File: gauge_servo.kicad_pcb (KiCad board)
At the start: 4 copper layers, 82 x 70 mm, 41 parts, among them J1 Servo 1, J10 LIM1, J11 LIM2, J12 NPX1, J3 Servo 2, J4 I2C, J5 STEPPER, J6 INPUT_1, J7 NPX2, J8 INPUT_2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

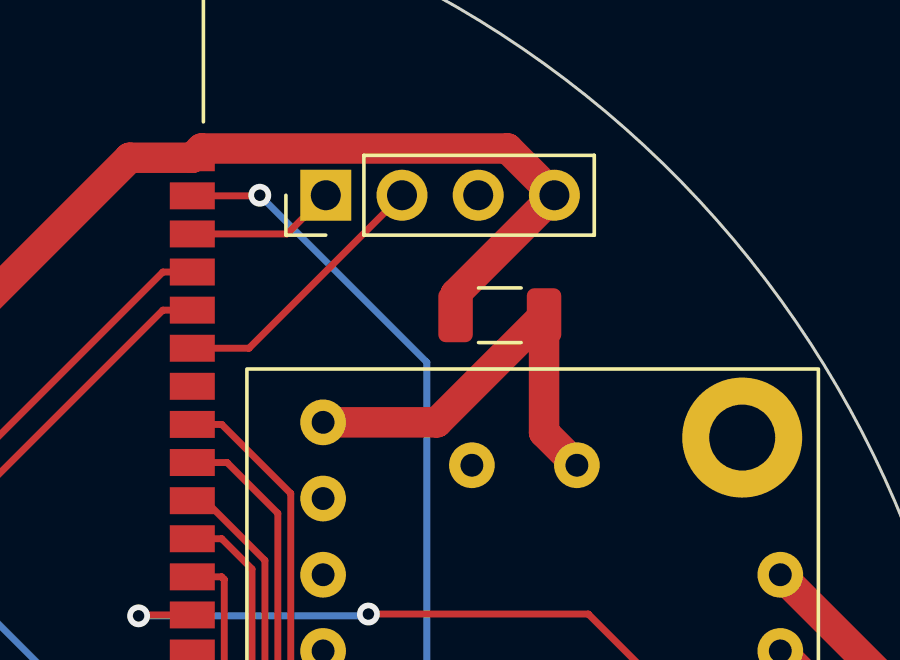
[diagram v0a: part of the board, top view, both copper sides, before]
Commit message: Fixed pinout error or Adafruit TB6612 custom component that caused short between 5V and gnd
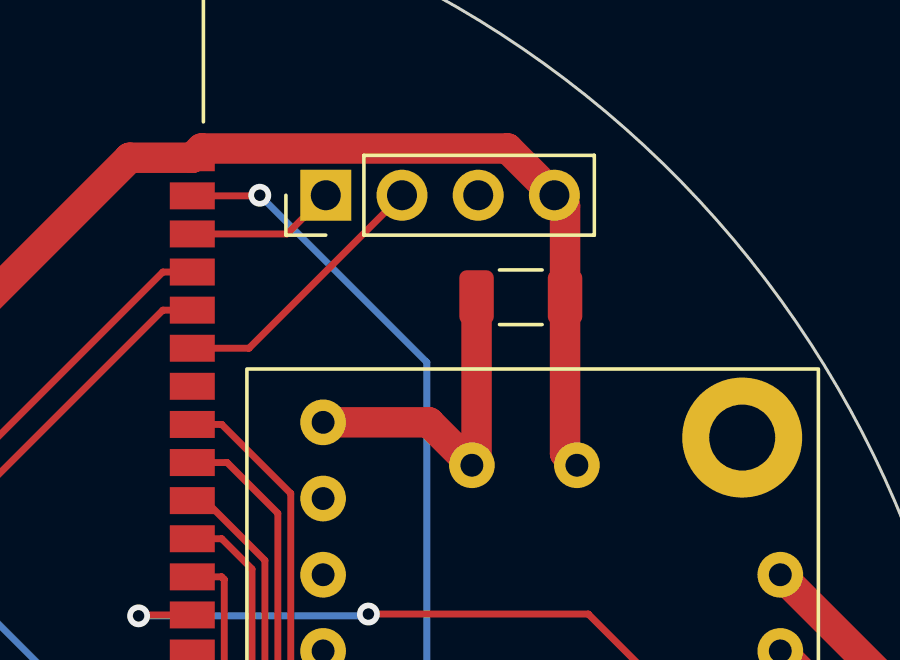
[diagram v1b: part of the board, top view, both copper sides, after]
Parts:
- moved C4 0.92 mm to (169.7, 79.4), turned to 0 degrees
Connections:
- U3 pad 17: +5V -> GND
- U3 pad 18: GND -> +5V
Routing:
- net GND: track 108.9 -> 112.9 mm
- net +5V: track 90.3 -> 87.2 mm
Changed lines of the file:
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@@
   )
   (footprint "Capacitor_SMD:C_1206_3216Metric" (layer "F.Cu")
-    (at 169 80 180)
+    (at 169.7 79.4)
     (descr "Capacitor SMD 1206 (3216 Metric), square (rectangular) end terminal, IPC_7351 nominal, (Body size source: IPC-SM-782 page 76, https://www.pcb-3d.com/wordpress/wp-content/uploads/ipc-sm-782a_amendment_1_and_2.pdf), generated with kicad-footprint-generator")
     (tags "capacitor")
@@
     (fp_line (start 1.6 -0.8) (end 1.6 0.8) (layer "F.Fab") (width 0.1))
     (fp_line (start -1.6 -0.8) (end 1.6 -0.8) (layer "F.Fab") (width 0.1))
-    (pad "1" smd roundrect (at -1.475 0 180) (size 1.15 1.8) (layers "F.Cu" "F.Paste" "F.Mask") (roundrect_rratio 0.217391)
+    (pad "1" smd roundrect (at -1.475 0) (size 1.15 1.8) (layers "F.Cu" "F.Paste" "F.Mask") (roundrect_rratio 0.217391)
       (net 3 "+5V") (pintype "passive"))
-    (pad "2" smd roundrect (at 1.475 0 180) (size 1.15 1.8) (layers "F.Cu" "F.Paste" "F.Mask") (roundrect_rratio 0.217391)
+    (pad "2" smd roundrect (at 1.475 0) (size 1.15 1.8) (layers "F.Cu" "F.Paste" "F.Mask") (roundrect_rratio 0.217391)
       (net 2 "GND") (pintype "passive"))
     (model "${KICAD6_3DMODEL_DIR}/Capacitor_SMD.3dshapes/C_1206_3216Metric.wrl"
@@
       (net 45 "Net-(J5-Pad4)") (pinfunction "MOTOR_B1") (pintype "output"))
     (pad "17" thru_hole circle (at 11 -10) (size 1.524 1.524) (drill 0.762) (layers *.Cu *.Mask)
-      (net 3 "+5V") (pinfunction "VMOTOR+") (pintype "power_in"))
-    (pad "18" thru_hole circle (at 7.5 -10) (size 1.524 1.524) (drill 0.762) (layers *.Cu *.Mask)
       (net 2 "GND") (pinfunction "VMOTOR-") (pintype "power_in"))
+    (pad "18" thru_hole circle (at 7.5 -10) (size 1.524 1.524) (drill 0.762) (layers *.Cu *.Mask)
+      (net 3 "+5V") (pinfunction "VMOTOR+") (pintype "power_in"))
   )
   (footprint "Package_TO_SOT_SMD:SOT-23" (layer "F.Cu")
@@
   (segment (start 141 123.475) (end 144 123.475) (width 1.016) (layer "F.Cu") (net 2))
   (segment (start 140.475 124) (end 141 123.475) (width 1.016) (layer "F.Cu") (net 2))
+  (segment (start 171.175 79.4) (end 171.175 84.605) (width 1.016) (layer "F.Cu") (net 2))
   (segment (start 156.66 74.75) (end 149.32 82.09) (width 1.016) (layer "F.Cu") (net 2))
   (segment (start 132.525 110) (end 135 107.525) (width 1.016) (layer "F.Cu") (net 2))
   (segment (start 158.75 74.75) (end 159.058 74.442) (width 1.016) (layer "F.Cu") (net 2))
+  (segment (start 171.175 84.605) (end 171.57 85) (width 1.016) (layer "F.Cu") (net 2))
+  (segment (start 171.175 79.4) (end 171.175 76.355) (width 1.016) (layer "F.Cu") (net 2))
   (segment (start 134.3 74.025) (end 135 74.725) (width 1.016) (layer "F.Cu") (net 2))
   (segment (start 135 74.725) (end 141.225 74.725) (width 1.016) (layer "F.Cu") (net 2))
@@
   (segment (start 133.225 81) (end 133.225 84.465) (width 1.016) (layer "F.Cu") (net 2))
   (segment (start 135 107.525) (end 136.267 107.525) (width 1.016) (layer "F.Cu") (net 2))
+  (segment (start 171.175 76.355) (end 170.82 76) (width 1.016) (layer "F.Cu") (net 2))
   (segment (start 169.262 74.442) (end 170.82 76) (width 1.016) (layer "F.Cu") (net 2))
-  (segment (start 167.525 80) (end 167.525 79.295) (width 1.016) (layer "F.Cu") (net 2))
   (segment (start 121.445 96) (end 129 96) (width 1.016) (layer "F.Cu") (net 2))
   (segment (start 158.75 74.75) (end 156.66 74.75) (width 1.016) (layer "F.Cu") (net 2))
@@
   (segment (start 141.225 74.725) (end 141.25 74.75) (width 1.016) (layer "F.Cu") (net 2))
   (segment (start 136.267 107.525) (end 138.856 104.936) (width 1.016) (layer "F.Cu") (net 2))
-  (segment (start 167.525 79.295) (end 170.82 76) (width 1.016) (layer "F.Cu") (net 2))
   (segment (start 130.825 110) (end 132.525 110) (width 1.016) (layer "F.Cu") (net 2))
   (segment (start 133 74.025) (end 134.3 74.025) (width 1.016) (layer "F.Cu") (net 2))
@@
   (segment (start 167.55 101.65) (end 167.55 104.55) (width 1.016) (layer "B.Cu") (net 2))
   (segment (start 120 94.555) (end 127.095 101.65) (width 1.016) (layer "B.Cu") (net 2))
-  (segment (start 166.905 83.57) (end 170.475 80) (width 1.016) (layer "F.Cu") (net 3))
   (segment (start 148.921 115.604) (end 157.398 115.604) (width 1.016) (layer "F.Cu") (net 3))
   (segment (start 144 120.525) (end 148.921 115.604) (width 1.016) (layer "F.Cu") (net 3))
   (segment (start 163.3 114.825) (end 165 116.525) (width 1.016) (layer "F.Cu") (net 3))
   (segment (start 138.15 119.4) (end 138.308 119.242) (width 1.016) (layer "F.Cu") (net 3))
-  (segment (start 163.11 83.57) (end 166.905 83.57) (width 1.016) (layer "F.Cu") (net 3))
+  (segment (start 168.225 84.845) (end 168.07 85) (width 1.016) (layer "F.Cu") (net 3))
   (segment (start 162 114.825) (end 160 114.825) (width 1.016) (layer "F.Cu") (net 3))
   (segment (start 159.637 110.825) (end 157.398 113.064) (width 1.016) (layer "F.Cu") (net 3))
   (segment (start 160 110.825) (end 159.637 110.825) (width 1.016) (layer "F.Cu") (net 3))
   (segment (start 142.717 119.242) (end 144 120.525) (width 1.016) (layer "F.Cu") (net 3))
-  (segment (start 170.475 83.905) (end 171.57 85) (width 1.016) (layer "F.Cu") (net 3))
+  (segment (start 163.11 83.57) (end 166.64 83.57) (width 1.016) (layer "F.Cu") (net 3))
+  (segment (start 168.225 79.4) (end 168.225 84.845) (width 1.016) (layer "F.Cu") (net 3))
   (segment (start 162 114.825) (end 163.3 114.825) (width 1.016) (layer "F.Cu") (net 3))
-  (segment (start 170.475 80) (end 170.475 83.905) (width 1.016) (layer "F.Cu") (net 3))
+  (segment (start 166.64 83.57) (end 168.07 85) (width 1.016) (layer "F.Cu") (net 3))
   (segment (start 138.308 119.242) (end 142.717 119.242) (width 1.016) (layer "F.Cu") (net 3))
   (via (at 172.92536 95) (size 3.048) (drill 1.524) (layers "F.Cu" "B.Cu") (net 3))

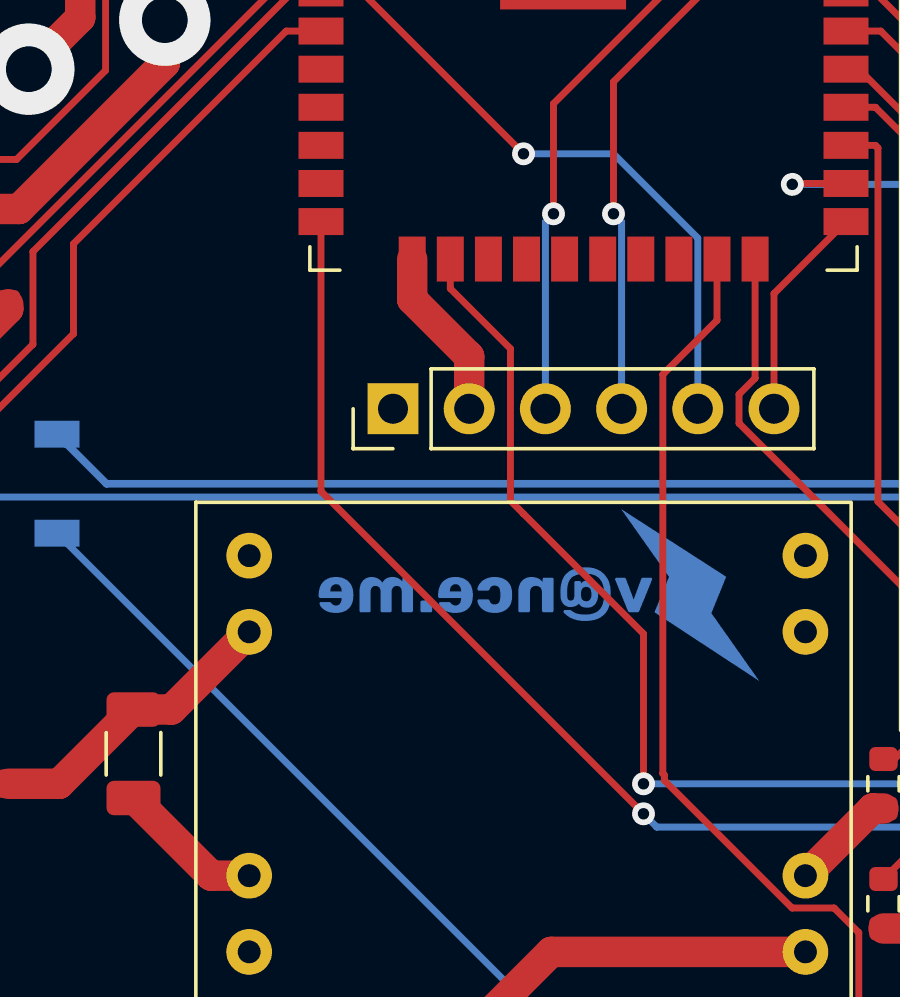
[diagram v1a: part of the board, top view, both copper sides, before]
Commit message: Moved LIMIT1 signal away from IO12 where the pullup was stopping the ESP from booting
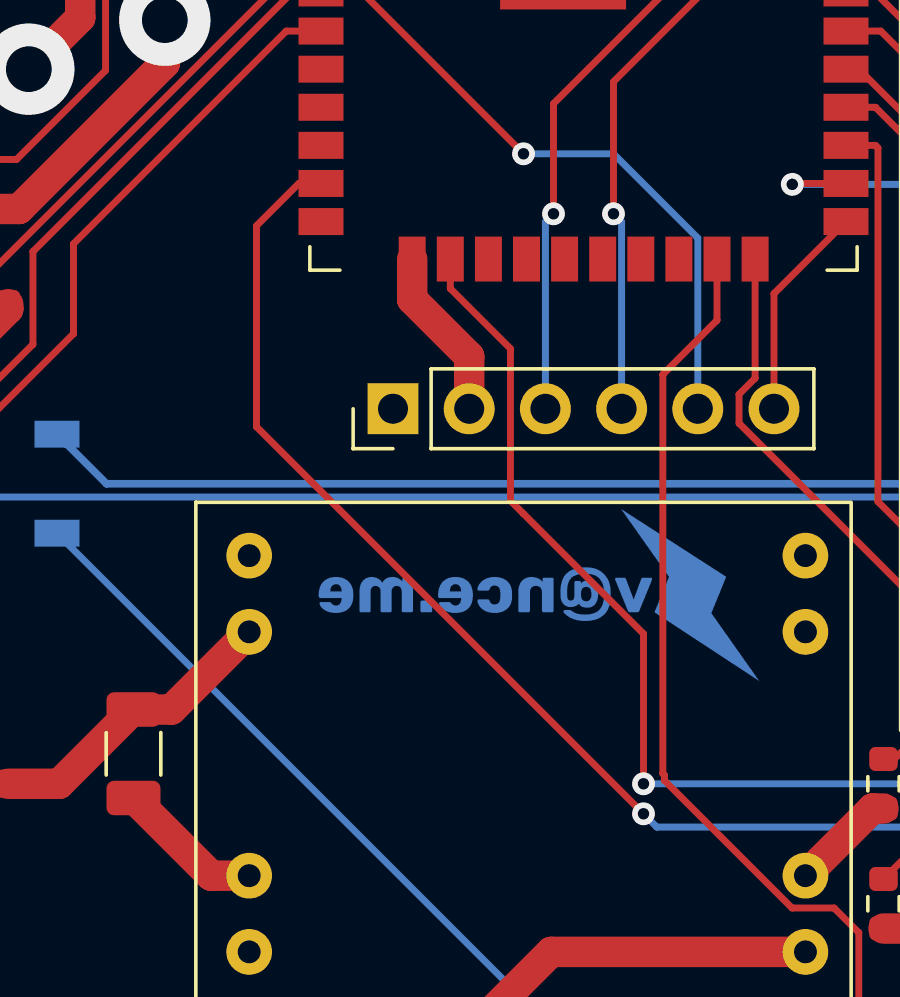
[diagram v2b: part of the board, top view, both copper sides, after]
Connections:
- U4 pad 13: unconnected-(U4-Pad13) -> LIMIT_1
- U4 pad 14: LIMIT_1 -> unconnected-(U4-Pad14)
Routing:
- net LIMIT_1: track 41.1 -> 44.6 mm
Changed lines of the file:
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@@
   (net 31 "unconnected-(U4-Pad11)")
   (net 32 "unconnected-(U4-Pad12)")
-  (net 33 "unconnected-(U4-Pad13)")
+  (net 33 "unconnected-(U4-Pad14)")
   (net 34 "unconnected-(U4-Pad17)")
   (net 35 "unconnected-(U4-Pad18)")
@@
       (net 32 "unconnected-(U4-Pad12)") (pinfunction "IO27") (pintype "bidirectional+no_connect"))
     (pad "13" smd rect (at -8.75 6.99) (size 1.5 0.9) (layers "F.Cu" "F.Paste" "F.Mask")
-      (net 33 "unconnected-(U4-Pad13)") (pinfunction "IO14") (pintype "bidirectional+no_connect"))
+      (net 41 "LIMIT_1") (pinfunction "IO14") (pintype "bidirectional"))
     (pad "14" smd rect (at -8.75 8.26) (size 1.5 0.9) (layers "F.Cu" "F.Paste" "F.Mask")
-      (net 41 "LIMIT_1") (pinfunction "IO12") (pintype "bidirectional"))
+      (net 33 "unconnected-(U4-Pad14)") (pinfunction "IO12") (pintype "bidirectional+no_connect"))
     (pad "15" smd rect (at -5.71 9.51 90) (size 1.5 0.9) (layers "F.Cu" "F.Paste" "F.Mask")
       (net 2 "GND") (pinfunction "GND") (pintype "passive"))
@@
   (segment (start 159.73114 88.72) (end 159.81557 88.80443) (width 0.23114) (layer "F.Cu") (net 27))
   (segment (start 159.81557 88.80443) (end 159.81557 100.59557) (width 0.23114) (layer "F.Cu") (net 27))
-  (segment (start 141.25 91.26) (end 141.25 100.25) (width 0.23114) (layer "F.Cu") (net 41))
-  (segment (start 141.25 100.25) (end 152 111) (width 0.23114) (layer "F.Cu") (net 41))
+  (segment (start 139.1 91.4) (end 140.51 89.99) (width 0.23114) (layer "F.Cu") (net 41))
+  (segment (start 140.51 89.99) (end 141.25 89.99) (width 0.23114) (layer "F.Cu") (net 41))
+  (segment (start 139.1 98.1) (end 139.1 91.4) (width 0.23114) (layer "F.Cu") (net 41))
   (segment (start 163.27 113.175) (end 165 111.445) (width 0.23114) (layer "F.Cu") (net 41))
   (segment (start 162 113.175) (end 163.27 113.175) (width 0.23114) (layer "F.Cu") (net 41))
+  (segment (start 152 111) (end 139.1 98.1) (width 0.23114) (layer "F.Cu") (net 41))
   (via (at 152 111) (size 0.762) (drill 0.381) (layers "F.Cu" "B.Cu") (net 41))
   (segment (start 152.445 111.445) (end 165 111.445) (width 0.23114) (layer "B.Cu") (net 41))
